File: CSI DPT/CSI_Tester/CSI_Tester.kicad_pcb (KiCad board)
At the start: 4 copper layers, 100 x 80 mm, 49 parts, among them J2 Conn_02x08_Odd_Even, J3 SSW-102-01-G-D, Q3 DMP3099L, U1 UCC23513QDWYRQ1, U2 MGJ2D121802SC, U4 LDK130-12_SOT23_SOT353, U5 NC7SZ125M5X, U7 ADM4168EBRUZ, U8 MGJ2D121802SC, U9 LT1086-ADJ

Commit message: CSI Tester V1 Completed
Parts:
- removed -18V1, 0V1, 0V2, 1.2V1, GND1A1, GND1B1, PWM_H1, VGATE_H1, VIN12V1, VIN5V1: TestPoint, TestPoint:TestPoint_Pad_D2.0mm
- removed C11: 0.1u, Capacitor_SMD:C_1206_3216Metric_Pad1.33x1.80mm_HandSolder
- removed C12: 10u, Capacitor_SMD:C_1206_3216Metric_Pad1.33x1.80mm_HandSolder
- removed C13: 10u, Gate_Driver:TAJB_AVX-M
- removed C14, C15: 10u, Capacitor_SMD:C_1206_3216Metric
- removed C5, C6, C7, C8, C9: 1u, Capacitor_SMD:C_1206_3216Metric
- removed D3: Z1SMAxxx, Diode_SMD:D_SMA_Handsoldering
- removed D4: D_Schottky, Diode_SMD:D_PowerDI-123
- removed H1, H2, H3: MountingHole, MountingHole:MountingHole_4.3mm_M4_DIN965
- removed HS_N1: HS_N, TestPoint:TestPoint_Pad_D2.0mm
- removed HS_P1: HS_P, TestPoint:TestPoint_Pad_D2.0mm
- removed LS_N1: LS_N, TestPoint:TestPoint_Pad_D2.0mm
- removed LS_P1: LS_P, TestPoint:TestPoint_Pad_D2.0mm
- removed Q3: DMP3099L, Package_TO_SOT_SMD:SOT-23
- removed R3, R4: 145, Resistor_SMD:R_1206_3216Metric_Pad1.30x1.75mm_HandSolder
- removed R6: 121, Resistor_SMD:R_1206_3216Metric_Pad1.30x1.75mm_HandSolder
- removed R7: 365, Resistor_SMD:R_1206_3216Metric_Pad1.30x1.75mm_HandSolder
- removed R8: 0, Resistor_SMD:R_1206_3216Metric_Pad1.30x1.75mm_HandSolder
- removed U1: UCC23513QDWYRQ1, Gate_Driver:SOIC06_SO-6_7P5X4P68_TEX-M
- removed U2, U8: MGJ2D121802SC, Converter_DCDC:Converter_DCDC_Murata_MGJ2DxxxxxxSC_THT
- removed U4: LDK130-12_SOT23_SOT353, Package_TO_SOT_SMD:SOT-23-5_HandSoldering
- removed U5: NC7SZ125M5X, Package_TO_SOT_SMD:SOT-23-5_HandSoldering
- removed U7: ADM4168EBRUZ, Gate_Driver:RU_16_ADI-M
- removed U9: LT1086-ADJ, Package_TO_SOT_SMD:TO-263-3_TabPin2
- added D1: UJ3N065025K3S, Package_TO_SOT_THT:TO-247-2_Vertical, F.Cu at (116.4, 112.3)
- added D2: UJ3N065025K3S, Package_TO_SOT_THT:TO-247-2_Vertical, F.Cu at (116.8, 76.5)
- added H4: MountingHole, MountingHole:MountingHole_4.3mm_M4_DIN965, F.Cu at (220.8, 47.5)
- added H5: MountingHole, MountingHole:MountingHole_4.3mm_M4_DIN965, F.Cu at (220.2, 136.2)
- added H6: MountingHole, MountingHole:MountingHole_4.3mm_M4_DIN965, F.Cu at (71.5, 47.5)
- added H7: MountingHole, MountingHole:MountingHole_4.3mm_M4_DIN965, F.Cu at (71.8, 136.2)
- added J1: TSM-102-01-SM-DV, VSI_DPT:SAMTEC_TSM-102-01-SM-DV, F.Cu at (92.0, 106.9)
- added J4: 8196, CSI_DPT:CONN_8196_KEY, F.Cu at (90.2, 138.5)
- added Q1: UJ3N065025K3S, Package_TO_SOT_THT:TO-247-3_Vertical, F.Cu at (107.6, 112.3)
- added Q2: UJ3N065025K3S, Package_TO_SOT_THT:TO-247-3_Vertical, F.Cu at (107.8, 76.5)
- added R2: CVR, Resistor_THT:CVR_SSDN005, F.Cu at (144.0, 68.0)
- added Vc+1: Vc+, TestPoint:TestPoint_Pad_D2.0mm, F.Cu at (145.0, 46.0)
- added Vc-1: TP1, TestPoint:TestPoint_Pad_D2.0mm, F.Cu at (145.0, 139.0)
- added Vcvr1: ~, TestPoint:TestPoint_Pad_D2.0mm, F.Cu at (137.0, 139.0)
- added Vcvr2: ~, TestPoint:TestPoint_Pad_D2.0mm, F.Cu at (137.0, 46.0)
- added Vdc+1: ~, TestPoint:TestPoint_Pad_D2.0mm, F.Cu at (129.0, 139.0)
- added Vdc+2: ~, TestPoint:TestPoint_Pad_D2.0mm, F.Cu at (129.0, 46.0)
- added Vg_H1: Vc+, TestPoint:TestPoint_Pad_D2.0mm, F.Cu at (112.0, 46.0)
- added Vg_L1: Vg_L, TestPoint:TestPoint_Pad_D2.0mm, F.Cu at (115.0, 139.0)
- added Vs_H1: Vc+, TestPoint:TestPoint_Pad_D2.0mm, F.Cu at (119.0, 46.0)
- added Vs_L1: Vc+, TestPoint:TestPoint_Pad_D2.0mm, F.Cu at (121.0, 139.0)
- C1, C2, C3, C4: value 1u -> 0.15u; footprint Capacitor_SMD:C_1206_3216Metric -> Capacitor_THT:C_Rect_L26.5mm_W10.5mm_P22.50mm_MKS4
- J2: value Conn_02x08_Odd_Even -> TSM-102-01-SM-DV; footprint Connector_IDC:IDC-Header_2x08_P2.54mm_Vertical -> VSI_DPT:SAMTEC_TSM-102-01-SM-DV
- J3: value SSW-102-01-G-D -> 8196; footprint Gate_Driver:CON4_2X2_TU_SSQ -> CSI_DPT:CONN_8196_KEY
- R1: value Ron 2 ohm -> CVR; footprint Resistor_SMD:R_1206_3216Metric_Pad1.30x1.75mm_HandSolder -> Resistor_THT:CVR_SSDN005; moved to F.Cu
- moved C4 91.3 mm to (218.0, 100.2), turned to 90 degrees
- moved J3 88.5 mm to (79.6, 45.1)
- moved C3 75.7 mm to (205.0, 100.2), turned to 90 degrees
- moved C1 63.6 mm to (179.0, 100.2), turned to 90 degrees
- moved C2 60.7 mm to (192.0, 100.2), turned to 90 degrees
- moved J2 29.7 mm to (92.0, 70.9), turned to 180 degrees
- moved R1 29.1 mm to (144.0, 110.0), turned to 0 degrees
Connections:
- net /Gate_Driver/0V_H renamed /Tester_Board/Vc+
- C1 pad 1: Net-(U4-EN) -> /Tester_Board/Vc-
- C2 pad 1: /Gate_Driver/1.2V_H -> /Tester_Board/Vc-
- C3 pad 1: /Gate_Driver/1.2V_H -> /Tester_Board/Vc-
- C4 pad 1: /Gate_Driver/1.2V_H -> /Tester_Board/Vc-
- J3 pad 1: /Gate_Driver/VGATE_H -> /Tester_Board/Vdc+
- J3 pad 2: /Gate_Driver/0V -> /Tester_Board/Vdc+
- J3 pad 3: /Gate_Driver/VGATE_H -> /Tester_Board/Vdc+
- J3 pad 4: /Gate_Driver/0V -> /Tester_Board/Vdc+
- R1 pad 1: /Gate_Driver/VGATE_H -> /Tester_Board/Vcvr1
- R1 pad 2: Net-(U1-VOUT) -> /Tester_Board/Vc-
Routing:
- net GND1: track 106.3 -> 0.00 mm, vias 5 -> 0
- net /Gate_Driver/LS_N: track 74.5 -> 0.00 mm, vias 1 -> 0
- net /Gate_Driver/VIN12V: track 72.9 -> 0.00 mm
- net /Gate_Driver/LS_P: track 70.6 -> 0.00 mm, vias 1 -> 0
- net /Tester_Board/Vs_L: track 0.00 -> 66.4 mm, vias 0 -> 1
- net /Gate_Driver/HS_P: track 63.1 -> 0.00 mm, vias 3 -> 0
- net /Gate_Driver/VIN5V: track 61.4 -> 0.00 mm, vias 24 -> 0
- net /Gate_Driver/HS_N: track 58.0 -> 0.00 mm, vias 1 -> 0
- net /Gate_Driver/-18V_H: track 51.7 -> 0.00 mm, vias 2 -> 0
- net /Tester_Board/Vg_H: track 0.00 -> 50.5 mm, vias 0 -> 1
- net /Tester_Board/Vc+: track 52.1 -> 3.00 mm, vias 0 -> 1
- net /Tester_Board/Vg_L: track 0.00 -> 47.8 mm, vias 0 -> 1
- net /Tester_Board/Vs_H: track 0.00 -> 47.7 mm, vias 0 -> 1
- net /Gate_Driver/PWM_H: track 34.3 -> 0.00 mm, vias 1 -> 0
- net /Gate_Driver/1.2V_H: track 28.1 -> 0.00 mm, vias 3 -> 0
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- added copper zone on B.Cu, net /Tester_Board/Vc+
- added copper zone on B.Cu, net /Tester_Board/Vc-
- added copper zone on F.Cu, net /Tester_Board/Vcvr1
- added copper zone on F.Cu, net /Tester_Board/Vcvr2
- added copper zone on In1.Cu, net /Tester_Board/Vdc+
- removed copper zone on In1.Cu, net /Gate_Driver/-18V_H
- removed copper zone on In1.Cu, net /Gate_Driver/0V
- removed copper zone on In1.Cu, net /Gate_Driver/1.2V_H
- removed copper zone on In2.Cu, net /Gate_Driver/VIN5V
- removed copper zone on In1.Cu, net GND1
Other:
- board size 100 x 80 mm -> 160 x 100 mm
- board text added: "CSI Double Pulse Tester V1 Hongyu Yan 2025/12/17"
- board text removed: "A"
- board text removed: "K"

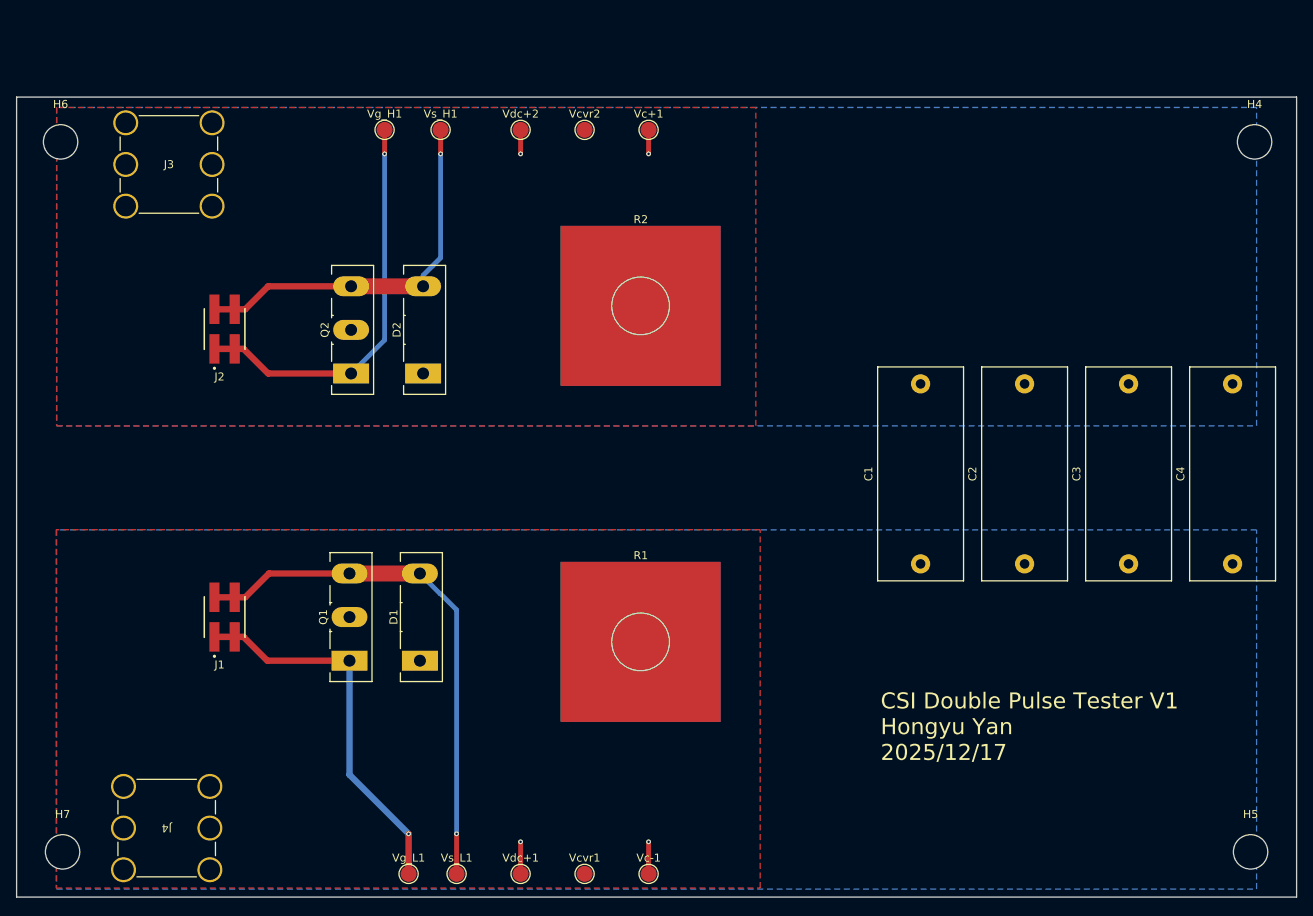
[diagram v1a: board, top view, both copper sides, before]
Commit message: Size down the boards
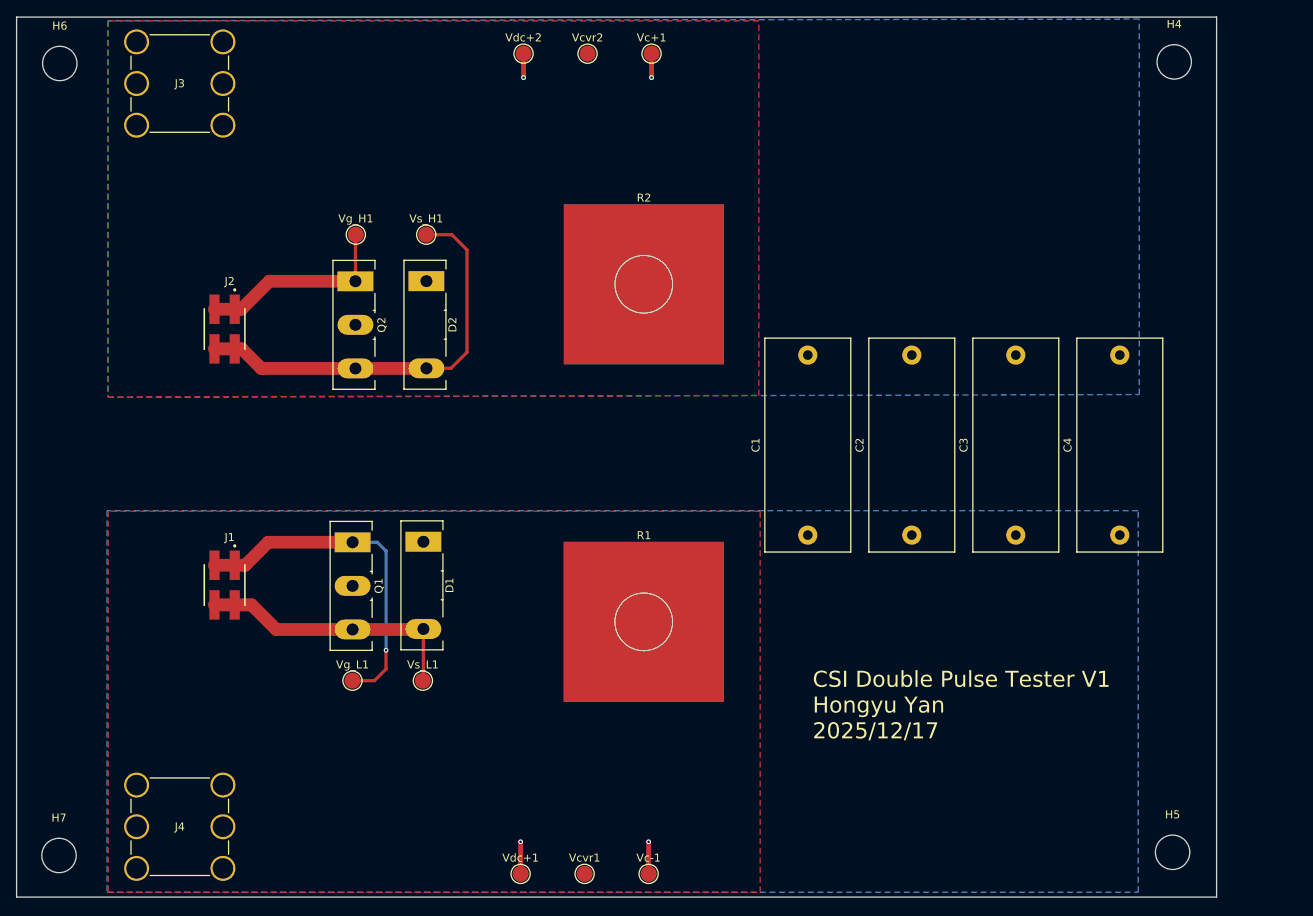
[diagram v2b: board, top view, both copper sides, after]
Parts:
- moved Vg_L1 25.1 mm to (108.0, 114.9)
- moved Vs_L1 24.5 mm to (116.8, 114.9)
- moved D1 14.9 mm to (116.9, 97.5), turned to -90 degrees
- moved Q1 14.8 mm to (108.0, 97.5), turned to -90 degrees
- moved C1 14.6 mm to (164.9, 96.7)
- moved C2 14.6 mm to (177.9, 96.7)
- moved C3 14.6 mm to (190.9, 96.7)
- moved C4 14.6 mm to (203.9, 96.7)
- moved H4 14.2 mm to (210.7, 37.5)
- moved J4 14.0 mm to (81.0, 127.9), turned to 0 degrees
- moved Vg_H1 13.6 mm to (108.4, 59.1)
- moved Vs_H1 13.2 mm to (117.2, 59.1)
- moved D2 11.5 mm to (117.2, 64.9), turned to -90 degrees
- moved Q2 11.5 mm to (108.4, 64.9), turned to -90 degrees
- moved J3 10.2 mm to (81.0, 35.0)
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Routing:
- net /Tester_Board/Vs_L: track 66.4 -> 33.9 mm, vias 1 -> 0
- net /Tester_Board/Vg_H: track 50.5 -> 24.9 mm, vias 1 -> 0
- net /Tester_Board/Vg_L: track 47.8 -> 42.7 mm
- net /Tester_Board/Vs_H: track 47.7 -> 52.1 mm, vias 1 -> 0
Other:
- board size 160 x 100 mm -> 150 x 110 mm
